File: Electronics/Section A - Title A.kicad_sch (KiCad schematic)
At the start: 9 parts, among them J2 THD-02-R, J3 Conn_01x22_Female, J4 690-019-298-412, U2 RT9742SNGV

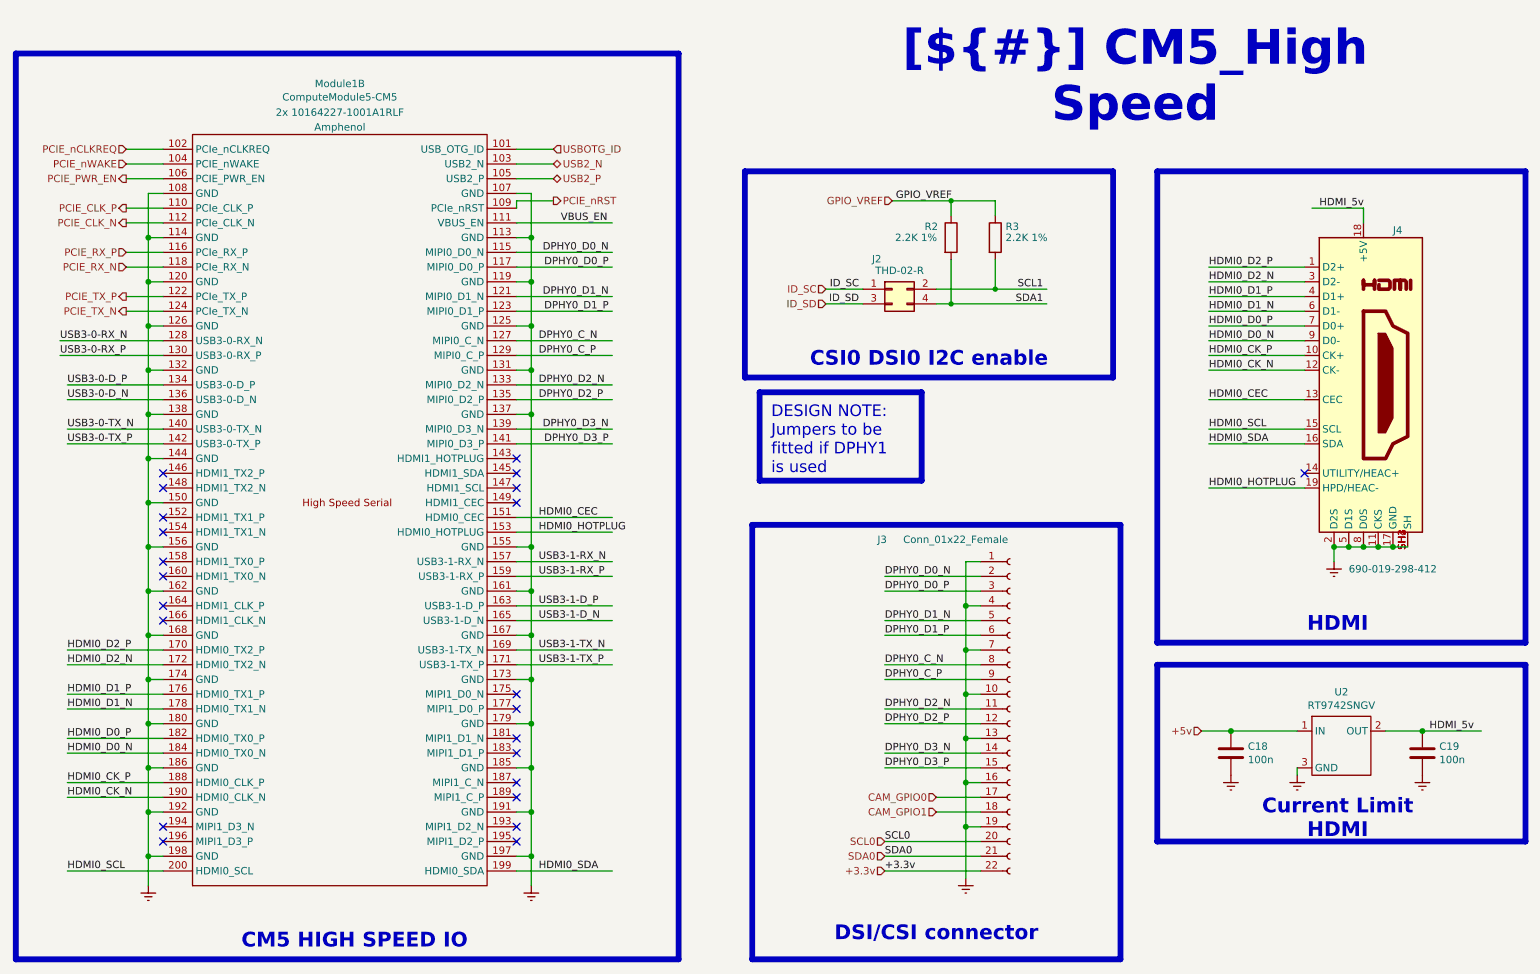
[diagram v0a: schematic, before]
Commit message: Rp2040 Power Sequence finished and general cleaning
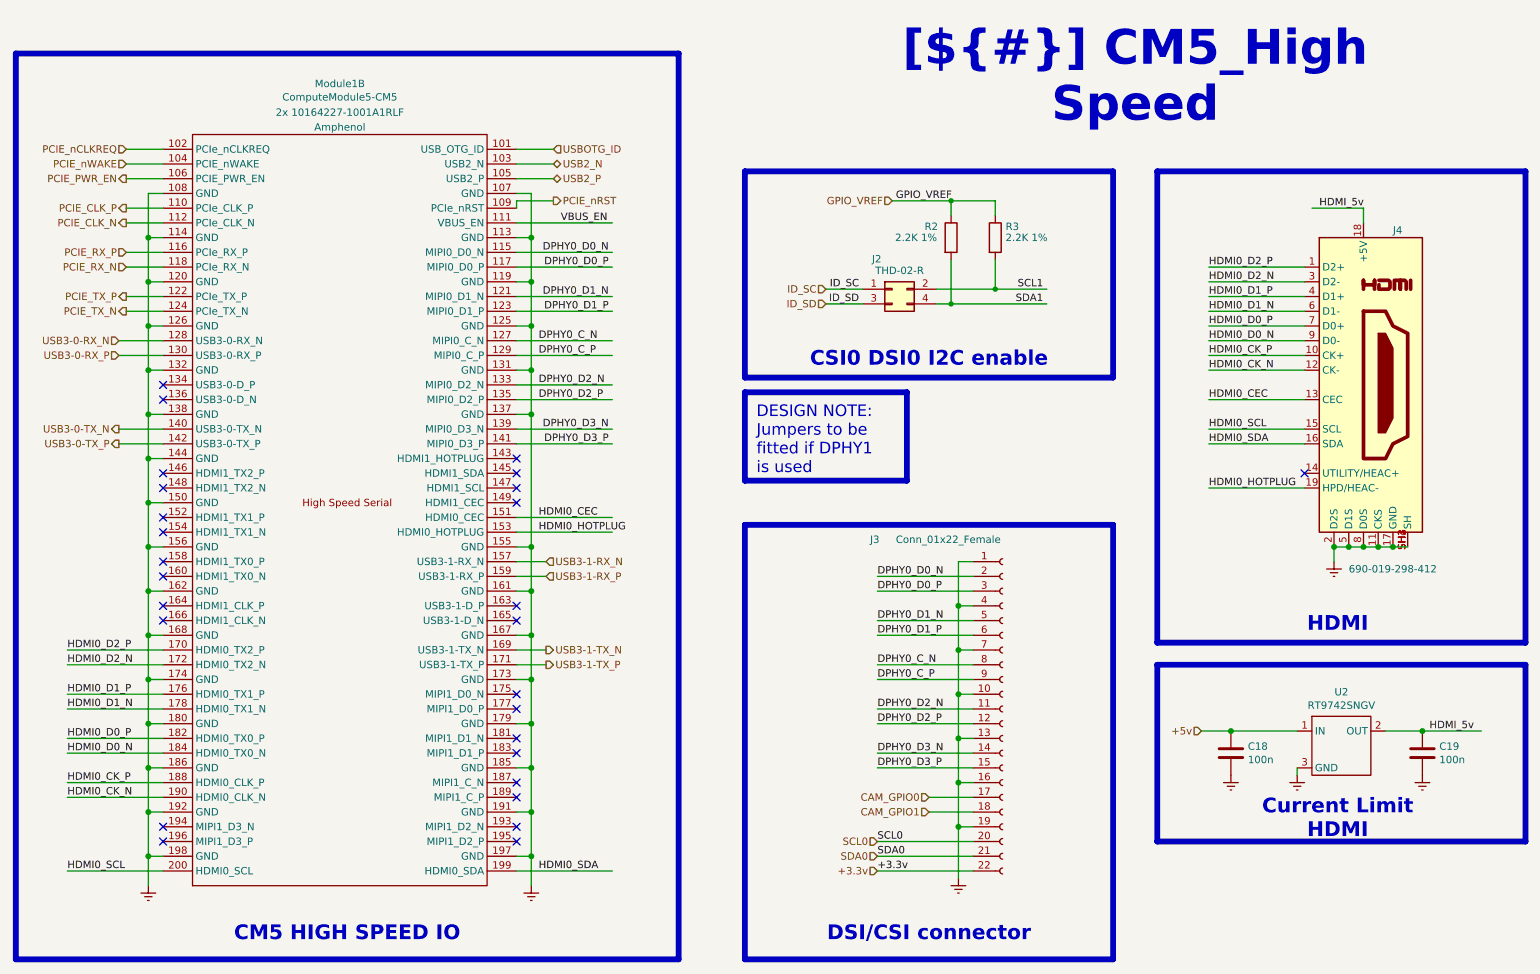
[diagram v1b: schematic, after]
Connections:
- net USB3-0-D_N: no longer names the net of Module1.136 (USB3-0-D_N)
- net USB3-0-D_P: no longer names the net of Module1.134 (USB3-0-D_P)
- net USB3-1-D_N: no longer names the net of Module1.165 (USB3-1-D_N)
- net USB3-1-D_P: no longer names the net of Module1.163 (USB3-1-D_P)
- no-connect marks 23 -> 27
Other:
- moved on the sheet: J3

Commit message: Starting the Sheet connections
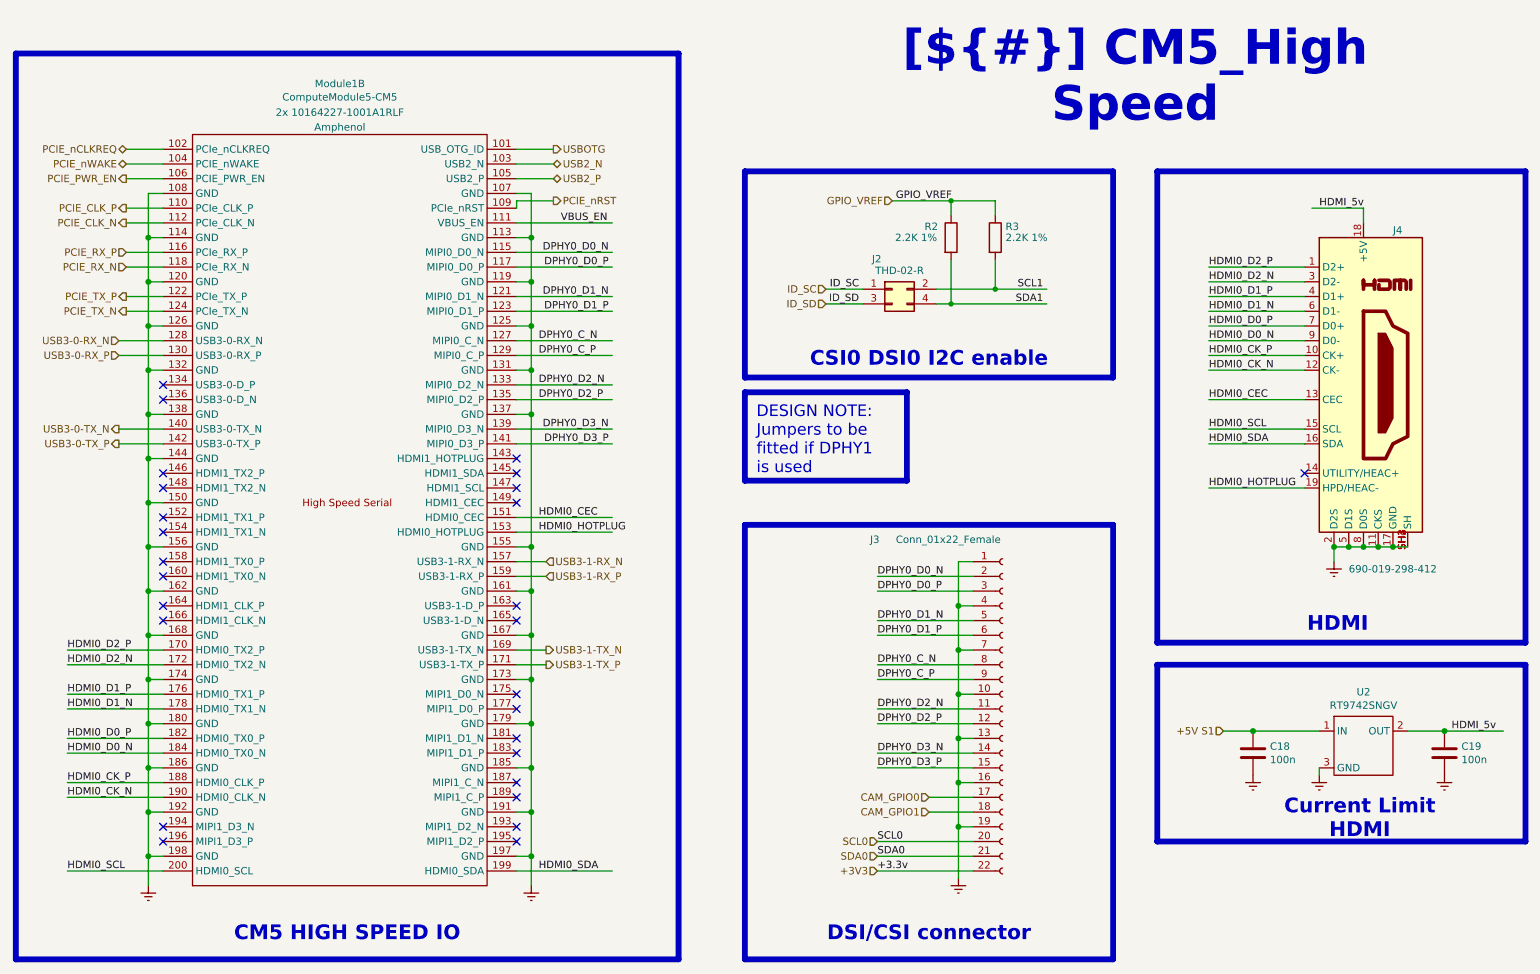
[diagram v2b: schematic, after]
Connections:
- net +3.3v renamed +3V3
- net +5v renamed +5V S1
- net USBOTG_ID renamed USBOTG
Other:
- moved on the sheet: C18, C19, U2

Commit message: Footprints Selected
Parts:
- removed J4: 690-019-298-412, CM5IO:EDAC 690-019-298-412, symbol CM5IO:HDMI_A_1.4
- added J3: HDMI_A, 10029449-111RLF:AMPHENOL_10029449-111RLF, symbol Connector:HDMI_A
- J2: renamed from J3; footprint CM5IO:Hirose_FH12-22S-0.5SH_1x22-1MP_P0.50mm_Horizontal -> Connector_FFC-FPC:Hirose_FH12-22S-0.5SH_1x22-1MP_P0.50mm_Horizontal
- Module1: footprint CM5IO:Raspberry-Pi-5-Compute-Module -> cm5:Raspberry-Pi-5-Compute-Module
- R1: renamed from R2; footprint Resistor_SMD:R_0402_1005Metric -> Resistor_SMD:R_0603_1608Metric
- R2: renamed from R3; footprint Resistor_SMD:R_0402_1005Metric -> Resistor_SMD:R_0603_1608Metric
- renumbered C18 to C1, C19 to C2, J2 to J1, U2 to U1
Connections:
- net HDMI0_CEC: now also J3.13 (CEC)
- net HDMI0_CK_N: now also J3.12 (CK-)
- net HDMI0_CK_P: now also J3.10 (CK+)
- net HDMI0_D0_N: now also J3.9 (D0-)
- net HDMI0_D0_P: now also J3.7 (D0+)
- net HDMI0_D1_N: now also J3.6 (D1-)
- net HDMI0_D1_P: now also J3.4 (D1+)
- net HDMI0_D2_N: now also J3.3 (D2-)
- net HDMI0_D2_P: now also J3.1 (D2+)
- net HDMI0_HOTPLUG: now also J3.19 (HPD)
- net HDMI0_SCL: now also J3.15 (SCL)
- net HDMI0_SDA: now also J3.16 (SDA)
- net HDMI_5v: now also J3.18 (+5V)
- new net: J3.11 (CKS), J3.17 (GND), J3.2 (D2S), J3.5 (D1S), J3.8 (D0S), J3.SH

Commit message: Footprints selected, Hiracicle connections created, Pcb next
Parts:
- C1, C2: footprint Capacitor_SMD:C_0402_1005Metric -> Capacitor_SMD:C_0603_1608Metric
- R1, R2: value 2.2K 1% -> 2K2 1%
- renumbered J3 to J2, J2 to J3
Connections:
- net gnd: now reaches J3.1 (Pin_1), J3.10 (Pin_10), J3.13 (Pin_13), J3.16 (Pin_16), J3.19 (Pin_19), J3.4 (Pin_4), J3.7 (Pin_7)
- net gnd: now also C1.2, C2.2, J2.11 (CKS), J2.17 (GND), J2.2 (D2S), J2.5 (D1S), J2.8 (D0S), J2.SH, Module1.107 (GND), Module1.108 (GND), Module1.113 (GND), Module1.114 (GND), Module1.119 (GND), Module1.120 (GND), Module1.125 (GND), Module1.126 (GND), Module1.131 (GND), Module1.132 (GND), Module1.137 (GND), Module1.138 (GND), Module1.144 (GND), Module1.150 (GND), Module1.155 (GND), Module1.156 (GND), Module1.161 (GND), Module1.162 (GND), Module1.167 (GND), Module1.168 (GND), Module1.173 (GND), Module1.174 (GND), Module1.179 (GND), Module1.180 (GND), Module1.185 (GND), Module1.186 (GND), Module1.191 (GND), Module1.192 (GND), Module1.197 (GND), Module1.198 (GND), U1.3 (GND)
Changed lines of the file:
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@@
 	(rectangle
 		(start 212.09 121.92)
-		(end 275.59 152.4)
+		(end 275.59 157.48)
 		(stroke
 			(width 1)
@@
 	(text_box "Current Limit HDMI"
 		(exclude_from_sim no)
-		(at 232.41 146.05 0)
+		(at 231.14 149.86 0)
 		(size 29.21 7.62)
 		(margins 1.9049 1.9049 1.9049 1.9049)
@@
 		(on_board yes)
 		(dnp no)
-		(property "Reference" "#PWR06"
+		(property "Reference" "#PWR01"
 			(at 242.57 110.49 0)
 			(effects
@@
 			)
 		)
-		(property "Value" "~"
+		(property "Value" "gnd"
 			(at 242.697 108.5342 0)
 			(effects
@@
 			(project "CM5 Nas"
 				(path "/0650c7a8-acba-429c-9f8e-eec0baf0bc1c/fede4c36-00cc-4d3d-b71c-5243ba232202/7d5a1283-086b-46b0-8df7-a9850521fb5e"
-					(reference "#PWR06")
+					(reference "#PWR01")
 					(unit 1)
 				)
@@
 		(on_board yes)
 		(dnp no)
-		(property "Reference" "#PWR02"
+		(property "Reference" "#PWR07"
 			(at 104.14 166.37 0)
 			(effects
@@
 			)
 		)
-		(property "Value" "~"
+		(property "Value" "gnd"
 			(at 104.267 164.4142 0)
 			(effects
@@
 			(project "CM5 Nas"
 				(path "/0650c7a8-acba-429c-9f8e-eec0baf0bc1c/fede4c36-00cc-4d3d-b71c-5243ba232202/7d5a1283-086b-46b0-8df7-a9850521fb5e"
-					(reference "#PWR02")
+					(reference "#PWR07")
 					(unit 1)
 				)
@@
 		(on_board yes)
 		(dnp no)
-		(property "Reference" "#PWR01"
+		(property "Reference" "#PWR06"
 			(at 38.1 166.37 0)
 			(effects
@@
 			)
 		)
-		(property "Value" "~"
+		(property "Value" "gnd"
 			(at 38.227 164.4142 0)
 			(effects
@@
 			(project "CM5 Nas"
 				(path "/0650c7a8-acba-429c-9f8e-eec0baf0bc1c/fede4c36-00cc-4d3d-b71c-5243ba232202/7d5a1283-086b-46b0-8df7-a9850521fb5e"
-					(reference "#PWR01")
+					(reference "#PWR06")
 					(unit 1)
 				)
@@
 		(on_board yes)
 		(dnp no)
-		(property "Reference" "#PWR03"
+		(property "Reference" "#PWR05"
 			(at 177.8 165.1 0)
 			(effects
@@
 			)
 		)
-		(property "Value" "~"
+		(property "Value" "gnd"
 			(at 177.927 163.1442 0)
 			(effects
@@
 			(project "CM5 Nas"
 				(path "/0650c7a8-acba-429c-9f8e-eec0baf0bc1c/fede4c36-00cc-4d3d-b71c-5243ba232202/7d5a1283-086b-46b0-8df7-a9850521fb5e"
-					(reference "#PWR03")
+					(reference "#PWR05")
 					(unit 1)
 				)
@@
 			)
 		)
-		(property "Value" "2.2K 1%"
+		(property "Value" "2K2 1%"
 			(at 166.878 48.26 0)
 			(effects
@@
 			)
 		)
-		(property "Value" "2.2K 1%"
+		(property "Value" "2K2 1%"
 			(at 185.928 48.26 0)
 			(effects
@@
 		(on_board yes)
 		(dnp no)
-		(property "Reference" "J2"
+		(property "Reference" "J3"
 			(at 162.56 100.33 0)
 			(effects
@@
 			(project "CM5 Nas"
 				(path "/0650c7a8-acba-429c-9f8e-eec0baf0bc1c/fede4c36-00cc-4d3d-b71c-5243ba232202/7d5a1283-086b-46b0-8df7-a9850521fb5e"
-					(reference "J2")
+					(reference "J3")
 					(unit 1)
 				)
@@
 			)
 		)
-		(property "Footprint" "Capacitor_SMD:C_0402_1005Metric"
+		(property "Footprint" "Capacitor_SMD:C_0603_1608Metric"
 			(at 262.5852 140.97 0)
 			(effects
@@
 			)
 		)
-		(property "Footprint" "Capacitor_SMD:C_0402_1005Metric"
+		(property "Footprint" "Capacitor_SMD:C_0603_1608Metric"
 			(at 229.5652 140.97 0)
 			(effects
@@
 		(on_board yes)
 		(dnp no)
-		(property "Reference" "#PWR07"
+		(property "Reference" "#PWR04"
 			(at 261.62 147.32 0)
 			(effects
@@
 			)
 		)
-		(property "Value" "~"
+		(property "Value" "gnd"
 			(at 261.747 145.3642 0)
 			(effects
@@
 			(project "CM5 Nas"
 				(path "/0650c7a8-acba-429c-9f8e-eec0baf0bc1c/fede4c36-00cc-4d3d-b71c-5243ba232202/7d5a1283-086b-46b0-8df7-a9850521fb5e"
-					(reference "#PWR07")
+					(reference "#PWR04")
 					(unit 1)
 				)
@@
 		(on_board yes)
 		(dnp no)
-		(property "Reference" "#PWR04"
+		(property "Reference" "#PWR02"
 			(at 228.6 147.32 0)
 			(effects
@@
 			)
 		)
-		(property "Value" "~"
+		(property "Value" "gnd"
 			(at 228.727 145.3642 0)
 			(effects
@@
 			(project "CM5 Nas"
 				(path "/0650c7a8-acba-429c-9f8e-eec0baf0bc1c/fede4c36-00cc-4d3d-b71c-5243ba232202/7d5a1283-086b-46b0-8df7-a9850521fb5e"
-					(reference "#PWR04")
+					(reference "#PWR02")
 					(unit 1)
 				)
@@
 		(on_board yes)
 		(dnp no)
-		(property "Reference" "#PWR05"
+		(property "Reference" "#PWR03"
 			(at 240.03 147.32 0)
 			(effects
@@
 			)
 		)
-		(property "Value" "~"
+		(property "Value" "gnd"
 			(at 240.157 145.3642 0)
 			(effects
@@
 			(project "CM5 Nas"
 				(path "/0650c7a8-acba-429c-9f8e-eec0baf0bc1c/fede4c36-00cc-4d3d-b71c-5243ba232202/7d5a1283-086b-46b0-8df7-a9850521fb5e"
-					(reference "#PWR05")
+					(reference "#PWR03")
 					(unit 1)
 				)
@@
 		(dnp no)
 		(fields_autoplaced yes)
-		(property "Reference" "J3"
+		(property "Reference" "J2"
 			(at 259.08 72.3899 0)
 			(effects
@@
 			(project ""
 				(path "/0650c7a8-acba-429c-9f8e-eec0baf0bc1c/fede4c36-00cc-4d3d-b71c-5243ba232202/7d5a1283-086b-46b0-8df7-a9850521fb5e"
-					(reference "J3")
+					(reference "J2")
 					(unit 1)
 				)

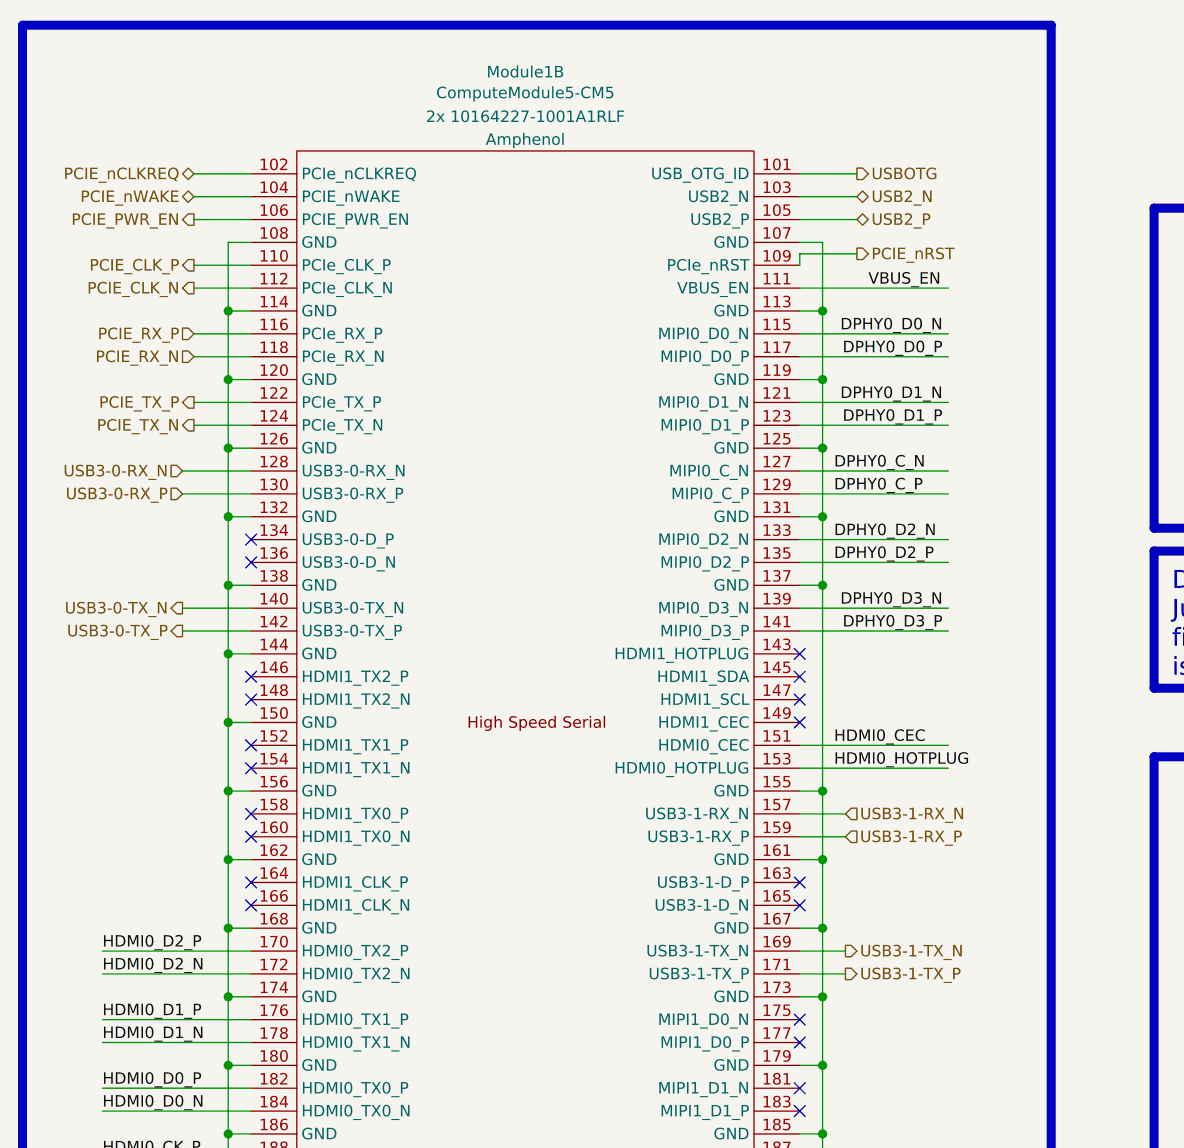
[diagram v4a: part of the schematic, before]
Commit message: Sata Port Changed
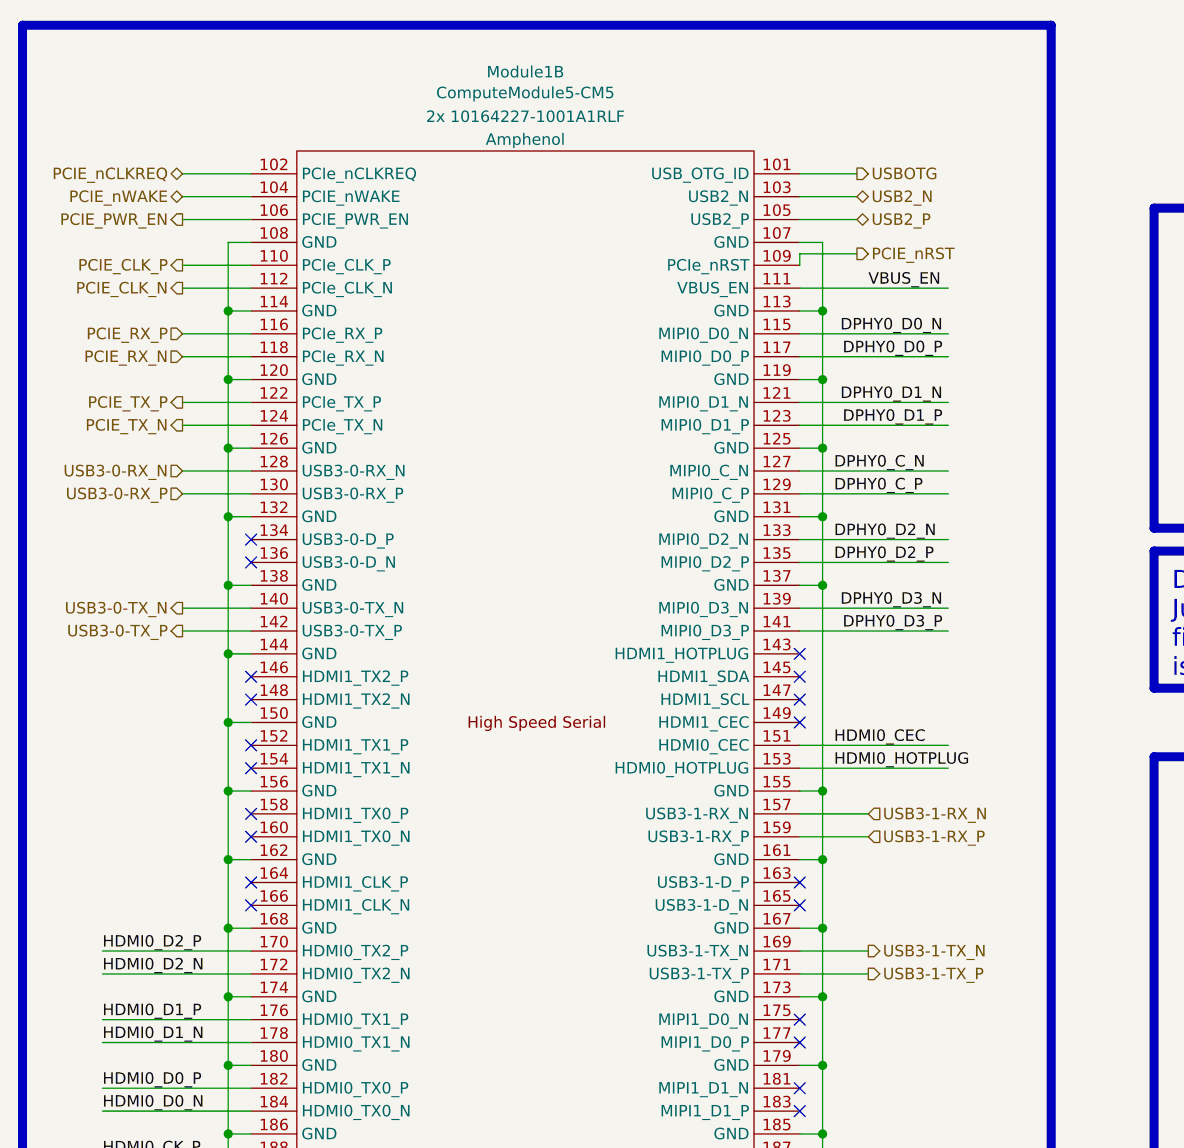
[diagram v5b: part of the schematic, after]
